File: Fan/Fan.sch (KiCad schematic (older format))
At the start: 5 parts, among them Q1 ZVN3306F

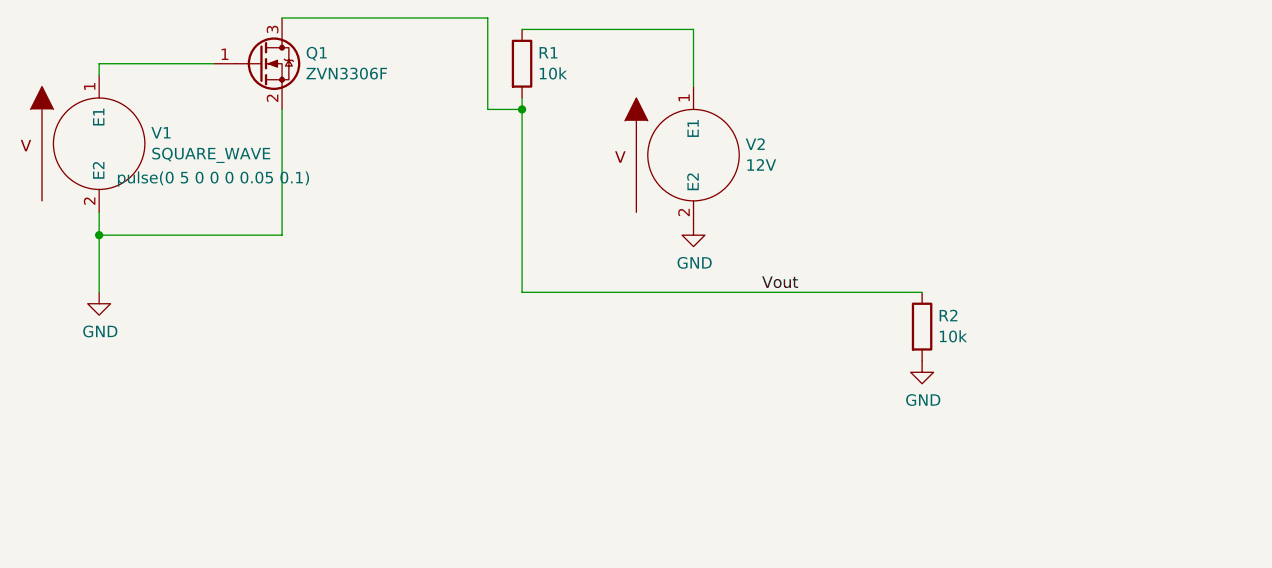
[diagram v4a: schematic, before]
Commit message: added fan system
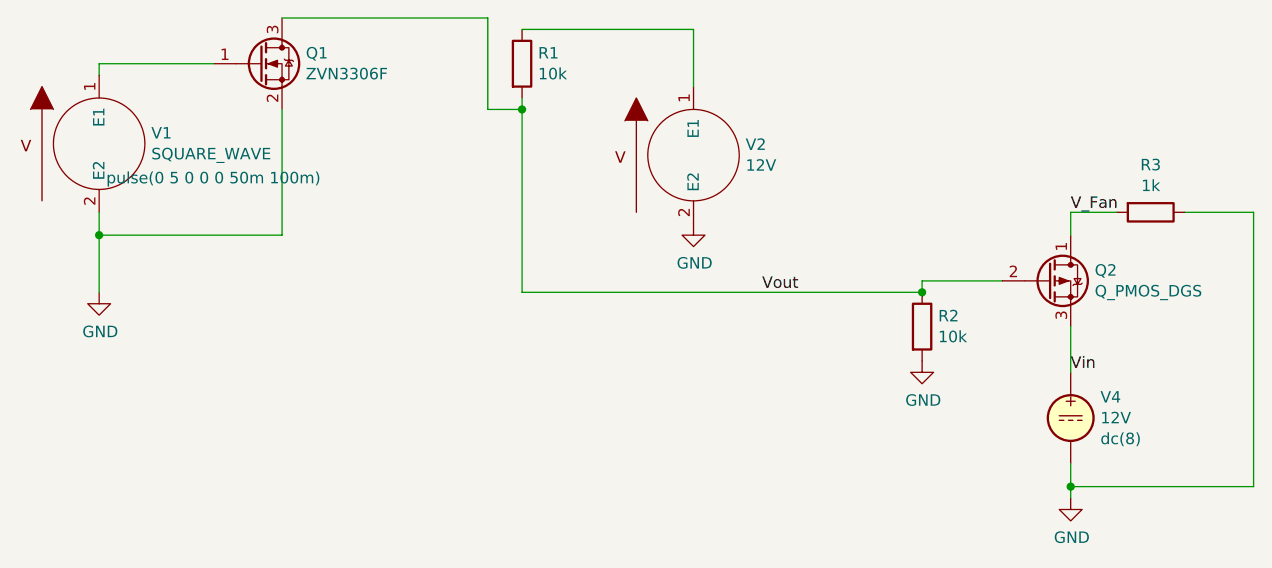
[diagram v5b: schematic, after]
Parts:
- added Q2: Q_PMOS_DGS, symbol Device:Q_PMOS_DGS
- added R3: 1k, symbol Device:R
- added V4: 12V, symbol Simulation_SPICE:VDC
- Q1: Spice_Lib_File (none) -> C:\\Users\\daich\\Desktop\\Solar Car\\ZVN3306F.spice.txt; Spice_Primitive M -> X
- V1: Spice_Model pulse(0 5 0 0 0 0.05 0.1) -> pulse(0 5 0 0 0 50m 100m)
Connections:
- net GND: now also R3.1, V4.2
- net Vout: now also Q2.2 (G)
- new net V_Fan: Q2.1 (D), R3.2
- new net Vin: Q2.3 (S), V4.1
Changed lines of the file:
@@
 F 3 "~" H 950 4150 50  0001 C CNN
 F 4 "V" H 950 4150 50  0001 C CNN "Spice_Primitive"
-F 5 "pulse(0 5 0 0 0 0.05 0.1)" H 1450 4000 50  0000 C CNN "Spice_Model"
+F 5 "pulse(0 5 0 0 0 50m 100m)" H 1450 4000 50  0000 C CNN "Spice_Model"
 F 6 "Y" H 950 4150 50  0001 C CNN "Spice_Netlist_Enabled"
 	1    950  4150
@@
 Wire Wire Line
 	1750 3600 2650 3600
-Wire Wire Line
-	2800 4800 4550 4800
 $Comp
 L Transistor_FET:ZVN3306F Q1
@@
 F 2 "Package_TO_SOT_SMD:SOT-23" H 1850 3725 50  0001 L CIN
 F 3 "http://www.diodes.com/assets/Datasheets/ZVN3306F.pdf" H 1650 3800 50  0001 L CNN
-F 4 "M" H 1650 3800 50  0001 C CNN "Spice_Primitive"
+F 4 "X" H 1650 3800 50  0001 C CNN "Spice_Primitive"
 F 5 "ZVN3306F" H 1650 3800 50  0001 C CNN "Spice_Model"
 F 6 "Y" H 1650 3800 50  0001 C CNN "Spice_Netlist_Enabled"
+F 7 "C:\\Users\\daich\\Desktop\\Solar Car\\ZVN3306F.spice.txt" H 1650 3800 50  0001 C CNN "Spice_Lib_File"
 	1    1650 3800
 	1    0    0    -1
@@
 	1    0    0    -1
 $EndComp
+Wire Wire Line
+	2800 4800 4550 4800
+Wire Wire Line
+	4550 4750 4550 4800
+Connection ~ 4550 4800
+Wire Wire Line
+	4550 4750 4900 4750
+$Comp
+L Device:R R3
+U 1 1 5EAE0EBF
+P 5550 4450
+F 0 "R3" V 5343 4450 50  0000 C CNN
+F 1 "1k" V 5434 4450 50  0000 C CNN
+F 2 "" V 5480 4450 50  0001 C CNN
+F 3 "~" H 5550 4450 50  0001 C CNN
+	1    5550 4450
+	0    1    1    0
+$EndComp
+$Comp
+L Simulation_SPICE:VDC V4
+U 1 1 5EAE25B8
+P 5200 5350
+F 0 "V4" H 5330 5441 50  0000 L CNN
+F 1 "12V" H 5330 5350 50  0000 L CNN
+F 2 "" H 5200 5350 50  0001 C CNN
+F 3 "~" H 5200 5350 50  0001 C CNN
+F 4 "Y" H 5200 5350 50  0001 L CNN "Spice_Netlist_Enabled"
+F 5 "V" H 5200 5350 50  0001 L CNN "Spice_Primitive"
+F 6 "dc(8)" H 5330 5259 50  0000 L CNN "Spice_Model"
+	1    5200 5350
+	1    0    0    -1
+$EndComp
+$Comp
+L power:GND #PWR05
+U 1 1 5EAE6962
+P 5200 5700
+F 0 "#PWR05" H 5200 5450 50  0001 C CNN
+F 1 "GND" H 5205 5527 50  0000 C CNN
+F 2 "" H 5200 5700 50  0001 C CNN
+F 3 "" H 5200 5700 50  0001 C CNN
+	1    5200 5700
+	1    0    0    -1
+$EndComp
+$Comp
+L Device:Q_PMOS_DGS Q2
+U 1 1 5EAE8255
+P 5100 4750
+F 0 "Q2" H 5305 4796 50  0000 L CNN
+F 1 "Q_PMOS_DGS" H 5305 4705 50  0000 L CNN
+F 2 "" H 5300 4850 50  0001 C CNN
+F 3 "~" H 5100 4750 50  0001 C CNN
+F 4 "X" H 5100 4750 50  0001 C CNN "Spice_Primitive"
+F 5 "ZVP3306A" H 5100 4750 50  0001 C CNN "Spice_Model"
+F 6 "Y" H 5100 4750 50  0001 C CNN "Spice_Netlist_Enabled"
+F 7 "C:\\Users\\daich\\Desktop\\Solar Car\\ZVP3306A.spice.txt" H 5100 4750 50  0001 C CNN "Spice_Lib_File"
+	1    5100 4750
+	1    0    0    -1
+$EndComp
+Wire Wire Line
+	5200 4450 5200 4550
+Wire Wire Line
+	5200 4950 5200 5150
+Wire Wire Line
+	5200 5550 5200 5650
+Text Label 5200 5150 0    50   ~ 0
+Vin
+Wire Wire Line
+	5200 4450 5400 4450
+Wire Wire Line
+	5700 4450 6000 4450
+Wire Wire Line
+	6000 4450 6000 5650
+Connection ~ 5200 5650
+Wire Wire Line
+	5200 5650 5200 5700
+Text Label 5200 4450 0    50   ~ 0
+V_Fan
+Wire Wire Line
+	5200 5650 6000 5650
 $EndSCHEMATC

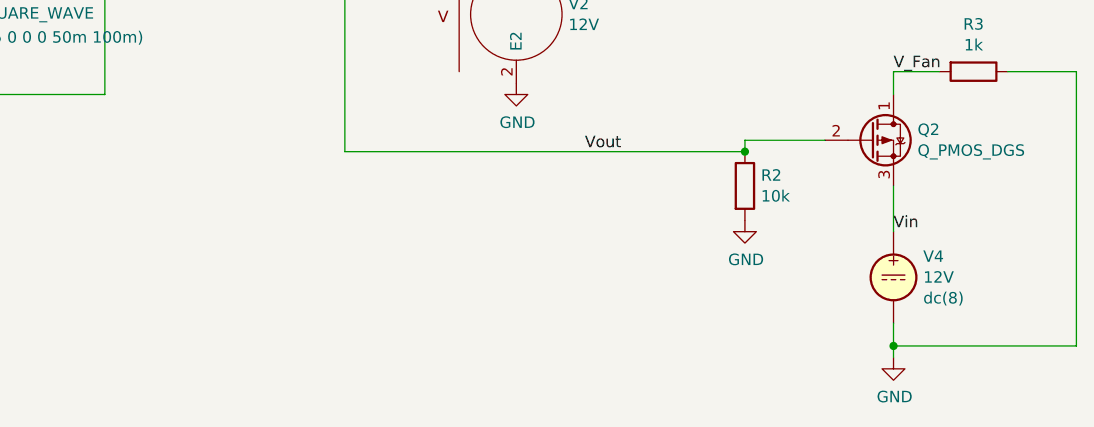
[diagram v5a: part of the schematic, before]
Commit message: made all paths to spice models relative and renumbered pins of MOSFETs in Fan
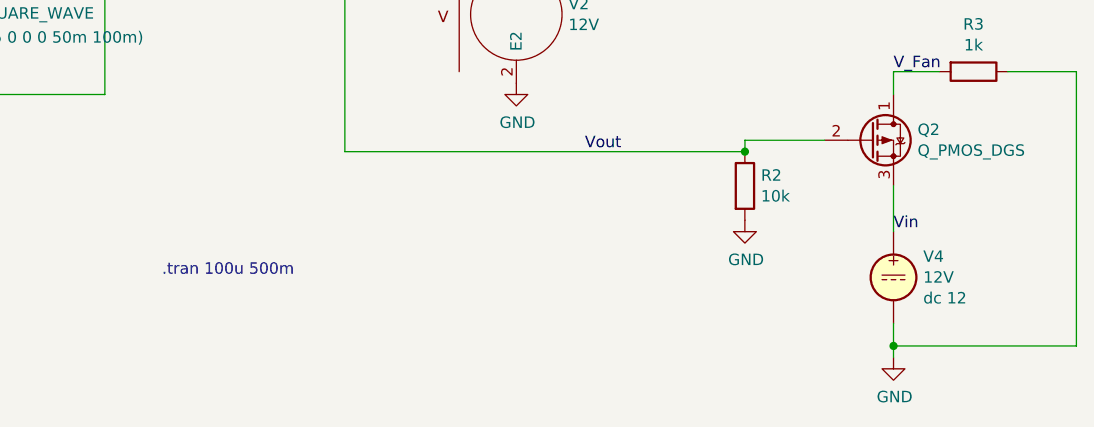
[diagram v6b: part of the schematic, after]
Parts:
- Q1: Spice_Lib_File C:\\Users\\daich\\Desktop\\Solar Car\\ZVN3306F.spice.txt -> ..\\ZVN3306F.spice; Spice_Node_Sequence (none) -> 3 1 2
- Q2: Spice_Lib_File C:\\Users\\daich\\Desktop\\Solar Car\\ZVP3306A.spice.txt -> ..\\ZVP3306A.spice; Spice_Node_Sequence (none) -> 1 2 3
- V4: Spice_Model dc(8) -> dc 12
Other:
- note added: ".tran 100u 500m"
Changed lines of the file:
@@
 F 5 "ZVN3306F" H 1650 3800 50  0001 C CNN "Spice_Model"
 F 6 "Y" H 1650 3800 50  0001 C CNN "Spice_Netlist_Enabled"
-F 7 "C:\\Users\\daich\\Desktop\\Solar Car\\ZVN3306F.spice.txt" H 1650 3800 50  0001 C CNN "Spice_Lib_File"
+F 7 "..\\ZVN3306F.spice" H 1650 3800 50  0001 C CNN "Spice_Lib_File"
+F 8 "3 1 2" H 1650 3800 50  0001 C CNN "Spice_Node_Sequence"
 	1    1650 3800
 	1    0    0    -1
@@
 F 4 "Y" H 5200 5350 50  0001 L CNN "Spice_Netlist_Enabled"
 F 5 "V" H 5200 5350 50  0001 L CNN "Spice_Primitive"
-F 6 "dc(8)" H 5330 5259 50  0000 L CNN "Spice_Model"
+F 6 "dc 12" H 5330 5259 50  0000 L CNN "Spice_Model"
 	1    5200 5350
 	1    0    0    -1
@@
 F 5 "ZVP3306A" H 5100 4750 50  0001 C CNN "Spice_Model"
 F 6 "Y" H 5100 4750 50  0001 C CNN "Spice_Netlist_Enabled"
-F 7 "C:\\Users\\daich\\Desktop\\Solar Car\\ZVP3306A.spice.txt" H 5100 4750 50  0001 C CNN "Spice_Lib_File"
+F 7 "..\\ZVP3306A.spice" H 5100 4750 50  0001 C CNN "Spice_Lib_File"
+F 8 "1 2 3" H 5100 4750 50  0001 C CNN "Spice_Node_Sequence"
 	1    5100 4750
 	1    0    0    -1
@@
 Wire Wire Line
 	5200 5650 6000 5650
+Text Notes 2000 5350 0    50   ~ 0
+.tran 100u 500m
 $EndSCHEMATC

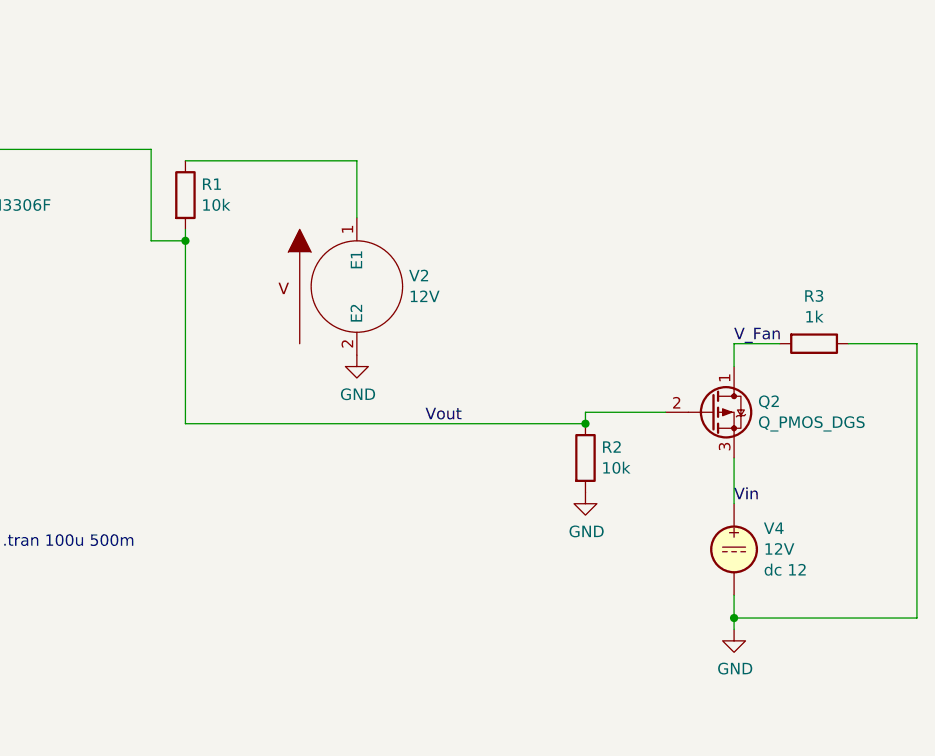
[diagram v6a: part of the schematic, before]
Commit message: Cleaned up Fan Schematic
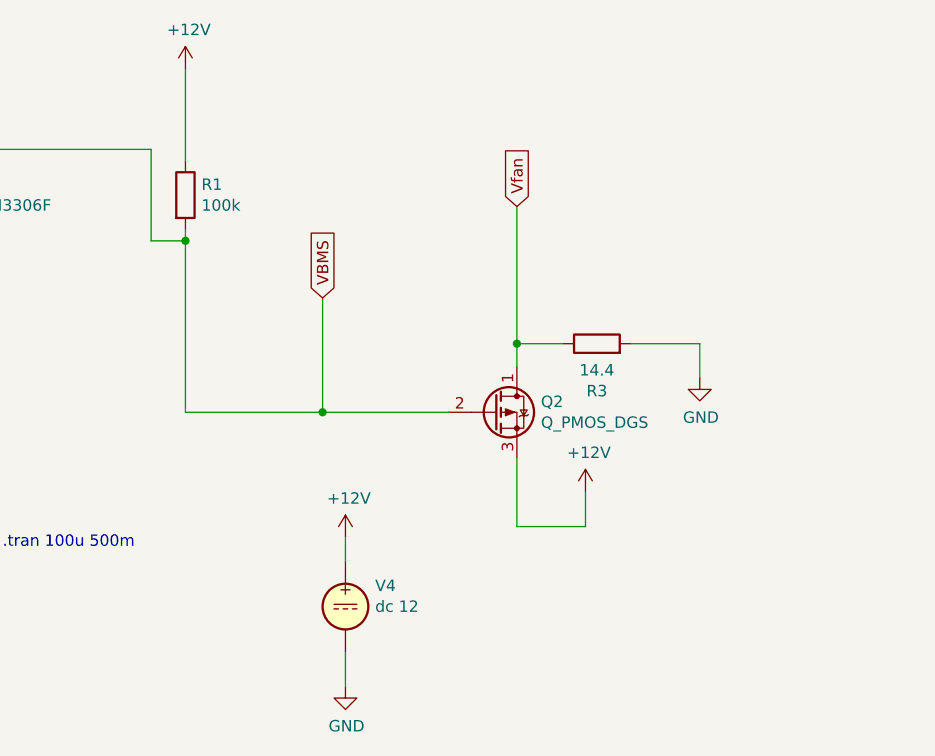
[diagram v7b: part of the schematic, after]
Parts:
- removed R2: 10k, symbol Device:R
- removed V2: 12V, symbol pspice:VSOURCE
- Q2: Spice_Node_Sequence 1 2 3 -> (none)
- R1: value 10k -> 100k
- R3: value 1k -> 14.4
- V4: value 12V -> dc 12; Spice_Model dc 12 -> (none)
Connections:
- net Vin is gone; now on net +12V: Q2.3 (S), V4.1
- net GND: now also R3.2; no longer R3.1
- net +12V: now reaches R1.1
- net V_Fan renamed Vfan
- net Vfan: now also R3.1; no longer R3.2
- net Vout renamed VBMS
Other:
- moved on the sheet: R3, V4
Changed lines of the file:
@@
 	1    0    0    -1
 $EndComp
-$Comp
-L Device:R R1
-U 1 1 5E93960D
-P 2800 3800
-F 0 "R1" H 2870 3846 50  0000 L CNN
-F 1 "10k" H 2870 3755 50  0000 L CNN
-F 2 "" V 2730 3800 50  0001 C CNN
-F 3 "~" H 2800 3800 50  0001 C CNN
-	1    2800 3800
-	1    0    0    -1
-$EndComp
-$Comp
-L pspice:VSOURCE V2
-U 1 1 5E93AC04
-P 3550 4200
-F 0 "V2" H 3778 4246 50  0000 L CNN
-F 1 "12V" H 3778 4155 50  0000 L CNN
-F 2 "" H 3550 4200 50  0001 C CNN
-F 3 "~" H 3550 4200 50  0001 C CNN
-F 4 "V" H 3550 4200 50  0001 C CNN "Spice_Primitive"
-F 5 "dc 12" H 3550 4200 50  0001 C CNN "Spice_Model"
-F 6 "Y" H 3550 4200 50  0001 C CNN "Spice_Netlist_Enabled"
-	1    3550 4200
-	1    0    0    -1
-$EndComp
-Wire Wire Line
-	3550 3900 3550 3650
-Wire Wire Line
-	3550 3650 2800 3650
 Wire Wire Line
 	950  3850 950  3800
@@
 Wire Wire Line
 	2650 4000 2800 4000
-Connection ~ 2800 4000
-Wire Wire Line
-	2800 4000 2800 4800
 Wire Wire Line
 	2650 3600 2650 4000
 Wire Wire Line
 	1750 3600 2650 3600
+$Comp
+L power:GND #PWR05
+U 1 1 5EAE6962
+P 3500 5950
+F 0 "#PWR05" H 3500 5700 50  0001 C CNN
+F 1 "GND" H 3505 5777 50  0000 C CNN
+F 2 "" H 3500 5950 50  0001 C CNN
+F 3 "" H 3500 5950 50  0001 C CNN
+	1    3500 5950
+	1    0    0    -1
+$EndComp
+Wire Wire Line
+	4250 4450 4250 4550
+Wire Wire Line
+	4250 4450 4450 4450
+Wire Wire Line
+	4750 4450 5050 4450
 $Comp
 L Transistor_FET:ZVN3306F Q1
@@
 	1    0    0    -1
 $EndComp
-Text Label 3850 4800 0    50   ~ 0
-Vout
+Text Notes 2000 5350 0    50   ~ 0
+.tran 100u 500m
 $Comp
-L power:GND #PWR02
-U 1 1 5E93E520
-P 3550 4500
-F 0 "#PWR02" H 3550 4250 50  0001 C CNN
-F 1 "GND" H 3555 4327 50  0000 C CNN
-F 2 "" H 3550 4500 50  0001 C CNN
-F 3 "" H 3550 4500 50  0001 C CNN
-	1    3550 4500
+L Simulation_SPICE:VDC V4
+U 1 1 5EAE25B8
+P 3500 5600
+F 0 "V4" H 3630 5691 50  0000 L CNN
+F 1 "dc 12" H 3630 5600 50  0000 L CNN
+F 2 "" H 3500 5600 50  0001 C CNN
+F 3 "~" H 3500 5600 50  0001 C CNN
+F 4 "Y" H 3500 5600 50  0001 L CNN "Spice_Netlist_Enabled"
+F 5 "V" H 3500 5600 50  0001 L CNN "Spice_Primitive"
+	1    3500 5600
+	1    0    0    -1
+$EndComp
+Wire Wire Line
+	3500 5300 3500 5400
+Text GLabel 3400 4250 1    50   Input ~ 0
+VBMS
+Text GLabel 4250 3850 1    50   Input ~ 0
+Vfan
+Wire Wire Line
+	4250 3850 4250 4450
+Connection ~ 4250 4450
+Wire Wire Line
+	3400 4750 3400 4250
+Wire Wire Line
+	2800 4750 2800 4000
+Connection ~ 2800 4000
+$Comp
+L Device:R R1
+U 1 1 5E93960D
+P 2800 3800
+F 0 "R1" H 2870 3846 50  0000 L CNN
+F 1 "100k" H 2870 3755 50  0000 L CNN
+F 2 "" V 2730 3800 50  0001 C CNN
+F 3 "~" H 2800 3800 50  0001 C CNN
+	1    2800 3800
+	1    0    0    -1
+$EndComp
+Wire Wire Line
+	2800 3250 2800 3650
+$Comp
+L power:+12V #PWR02
+U 1 1 5EBA4048
+P 2800 3250
+F 0 "#PWR02" H 2800 3100 50  0001 C CNN
+F 1 "+12V" H 2815 3423 50  0000 C CNN
+F 2 "" H 2800 3250 50  0001 C CNN
+F 3 "" H 2800 3250 50  0001 C CNN
+	1    2800 3250
 	1    0    0    -1
 $EndComp
 $Comp
-L Device:R R2
-U 1 1 5E9D1C4A
-P 4550 4950
-F 0 "R2" H 4620 4996 50  0000 L CNN
-F 1 "10k" H 4620 4905 50  0000 L CNN
-F 2 "" V 4480 4950 50  0001 C CNN
-F 3 "~" H 4550 4950 50  0001 C CNN
-	1    4550 4950
+L power:+12V #PWR03
+U 1 1 5EBA62CC
+P 3500 5300
+F 0 "#PWR03" H 3500 5150 50  0001 C CNN
+F 1 "+12V" H 3515 5473 50  0000 C CNN
+F 2 "" H 3500 5300 50  0001 C CNN
+F 3 "" H 3500 5300 50  0001 C CNN
+	1    3500 5300
 	1    0    0    -1
 $EndComp
 $Comp
-L power:GND #PWR03
-U 1 1 5E9D21C2
+L power:+12V #PWR04
+U 1 1 5EBA6764
 P 4550 5100
-F 0 "#PWR03" H 4550 4850 50  0001 C CNN
-F 1 "GND" H 4555 4927 50  0000 C CNN
+F 0 "#PWR04" H 4550 4950 50  0001 C CNN
+F 1 "+12V" H 4565 5273 50  0000 C CNN
 F 2 "" H 4550 5100 50  0001 C CNN
 F 3 "" H 4550 5100 50  0001 C CNN
@@
 	1    0    0    -1
 $EndComp
+$Comp
+L Device:Q_PMOS_DGS Q2
+U 1 1 5EBA07C8
+P 4150 4750
+F 0 "Q2" H 4355 4796 50  0000 L CNN
+F 1 "Q_PMOS_DGS" H 4355 4705 50  0000 L CNN
+F 2 "" H 4350 4850 50  0001 C CNN
+F 3 "~" H 4150 4750 50  0001 C CNN
+F 4 "X" H 4150 4750 50  0001 C CNN "Spice_Primitive"
+F 5 "ZVP3306A" H 4150 4750 50  0001 C CNN "Spice_Model"
+F 6 "Y" H 4150 4750 50  0001 C CNN "Spice_Netlist_Enabled"
+F 7 "..\\ZVP3306A.spice" H 4150 4750 50  0001 C CNN "Spice_Lib_File"
+	1    4150 4750
+	1    0    0    -1
+$EndComp
 Wire Wire Line
-	2800 4800 4550 4800
+	4250 5250 4550 5250
 Wire Wire Line
-	4550 4750 4550 4800
-Connection ~ 4550 4800
+	4550 5250 4550 5100
 Wire Wire Line
-	4550 4750 4900 4750
+	4250 4950 4250 5250
+$Comp
+L power:GND #PWR06
+U 1 1 5EBA7952
+P 5050 4600
+F 0 "#PWR06" H 5050 4350 50  0001 C CNN
+F 1 "GND" H 5055 4427 50  0000 C CNN
+F 2 "" H 5050 4600 50  0001 C CNN
+F 3 "" H 5050 4600 50  0001 C CNN
+	1    5050 4600
+	1    0    0    -1
+$EndComp
+Wire Wire Line
+	5050 4450 5050 4600
+Wire Wire Line
+	3500 5800 3500 5950
+Wire Wire Line
+	2800 4750 3400 4750
+Connection ~ 3400 4750
+Wire Wire Line
+	3400 4750 3950 4750
 $Comp
 L Device:R R3
 U 1 1 5EAE0EBF
-P 5550 4450
-F 0 "R3" V 5343 4450 50  0000 C CNN
-F 1 "1k" V 5434 4450 50  0000 C CNN
-F 2 "" V 5480 4450 50  0001 C CNN
-F 3 "~" H 5550 4450 50  0001 C CNN
-	1    5550 4450
-	0    1    1    0
+P 4600 4450
+F 0 "R3" V 4393 4450 50  0000 C CNN
+F 1 "14.4" V 4484 4450 50  0000 C CNN
+F 2 "" V 4530 4450 50  0001 C CNN
+F 3 "~" H 4600 4450 50  0001 C CNN
+	1    4600 4450
+	0    -1   -1   0
 $EndComp
-$Comp
-L Simulation_SPICE:VDC V4
-U 1 1 5EAE25B8
-P 5200 5350
-F 0 "V4" H 5330 5441 50  0000 L CNN
-F 1 "12V" H 5330 5350 50  0000 L CNN
-F 2 "" H 5200 5350 50  0001 C CNN
-F 3 "~" H 5200 5350 50  0001 C CNN
-F 4 "Y" H 5200 5350 50  0001 L CNN "Spice_Netlist_Enabled"
-F 5 "V" H 5200 5350 50  0001 L CNN "Spice_Primitive"
-F 6 "dc 12" H 5330 5259 50  0000 L CNN "Spice_Model"
-	1    5200 5350
-	1    0    0    -1
-$EndComp
-$Comp
-L power:GND #PWR05
-U 1 1 5EAE6962
-P 5200 5700
-F 0 "#PWR05" H 5200 5450 50  0001 C CNN
-F 1 "GND" H 5205 5527 50  0000 C CNN
-F 2 "" H 5200 5700 50  0001 C CNN
-F 3 "" H 5200 5700 50  0001 C CNN
-	1    5200 5700
-	1    0    0    -1
-$EndComp
-$Comp
-L Device:Q_PMOS_DGS Q2
-U 1 1 5EAE8255
-P 5100 4750
-F 0 "Q2" H 5305 4796 50  0000 L CNN
-F 1 "Q_PMOS_DGS" H 5305 4705 50  0000 L CNN
-F 2 "" H 5300 4850 50  0001 C CNN
-F 3 "~" H 5100 4750 50  0001 C CNN
-F 4 "X" H 5100 4750 50  0001 C CNN "Spice_Primitive"
-F 5 "ZVP3306A" H 5100 4750 50  0001 C CNN "Spice_Model"
-F 6 "Y" H 5100 4750 50  0001 C CNN "Spice_Netlist_Enabled"
-F 7 "..\\ZVP3306A.spice" H 5100 4750 50  0001 C CNN "Spice_Lib_File"
-F 8 "1 2 3" H 5100 4750 50  0001 C CNN "Spice_Node_Sequence"
-	1    5100 4750
-	1    0    0    -1
-$EndComp
-Wire Wire Line
-	5200 4450 5200 4550
-Wire Wire Line
-	5200 4950 5200 5150
-Wire Wire Line
-	5200 5550 5200 5650
-Text Label 5200 5150 0    50   ~ 0
-Vin
-Wire Wire Line
-	5200 4450 5400 4450
-Wire Wire Line
-	5700 4450 6000 4450
-Wire Wire Line
-	6000 4450 6000 5650
-Connection ~ 5200 5650
-Wire Wire Line
-	5200 5650 5200 5700
-Text Label 5200 4450 0    50   ~ 0
-V_Fan
-Wire Wire Line
-	5200 5650 6000 5650
-Text Notes 2000 5350 0    50   ~ 0
-.tran 100u 500m
 $EndSCHEMATC
